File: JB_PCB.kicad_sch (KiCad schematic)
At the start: 11 parts, among them J2 Screw_Terminal_01x02, J3 Screw_Terminal_01x02, J4 Screw_Terminal_01x02, J6 Screw_Terminal_01x02

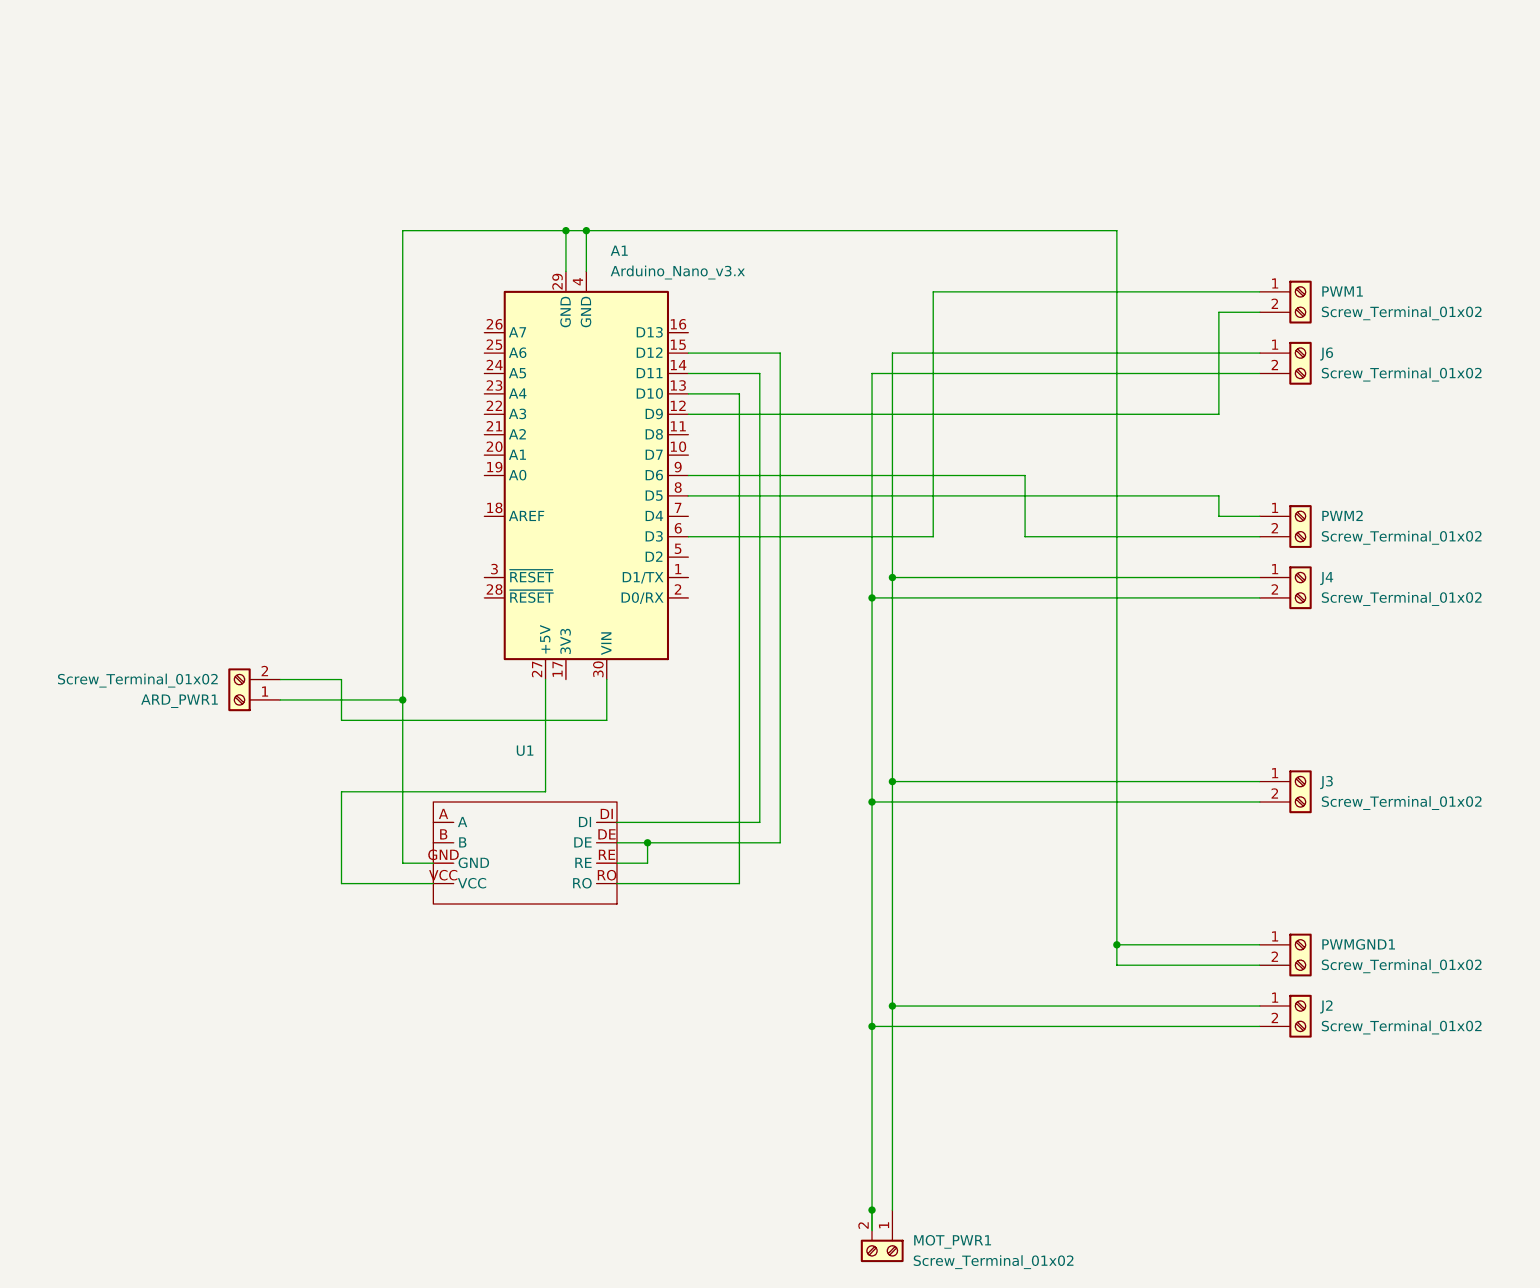
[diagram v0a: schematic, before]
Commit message: Added Servo pins
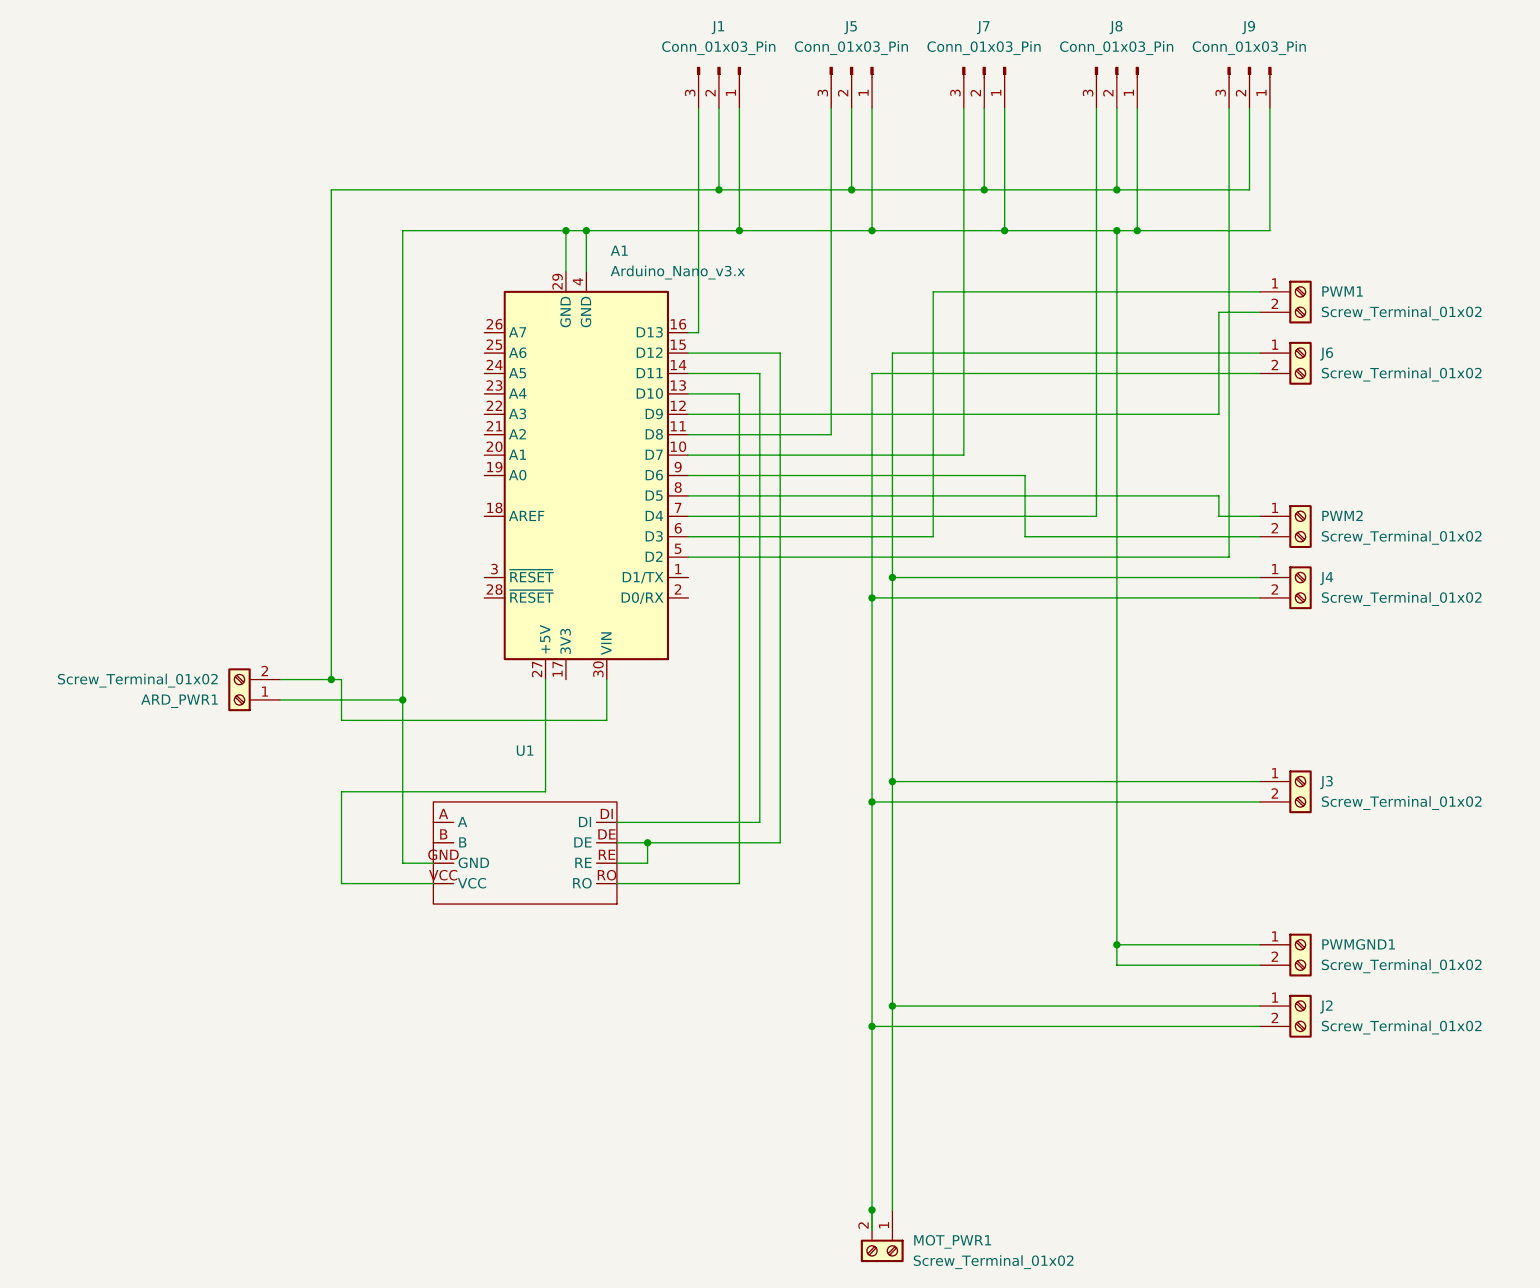
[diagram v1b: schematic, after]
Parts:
- added J1, J5, J7, J8, J9: Conn_01x03_Pin, myFootprints.pretty-master:3x1_Pin_Header, symbol Connector:Conn_01x03_Pin
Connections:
- net at A1.29 (GND), A1.4 (GND), ARD_PWR1.1 (Pin_1)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: now also J1.1 (Pin_1), J5.1 (Pin_1), J7.1 (Pin_1), J8.1 (Pin_1), J9.1 (Pin_1)
- net at A1.30 (VIN), ARD_PWR1.2 (Pin_2): now also J1.2 (Pin_2), J5.2 (Pin_2), J7.2 (Pin_2), J8.2 (Pin_2), J9.2 (Pin_2)
- net at A1.10 (D7): now also J7.3 (Pin_3)
- net at A1.11 (D8): now also J5.3 (Pin_3)
- net at A1.16 (D13): now also J1.3 (Pin_3)
- net at A1.5 (D2): now also J9.3 (Pin_3)
- net at A1.7 (D4): now also J8.3 (Pin_3)

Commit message: added pins for external PWM board
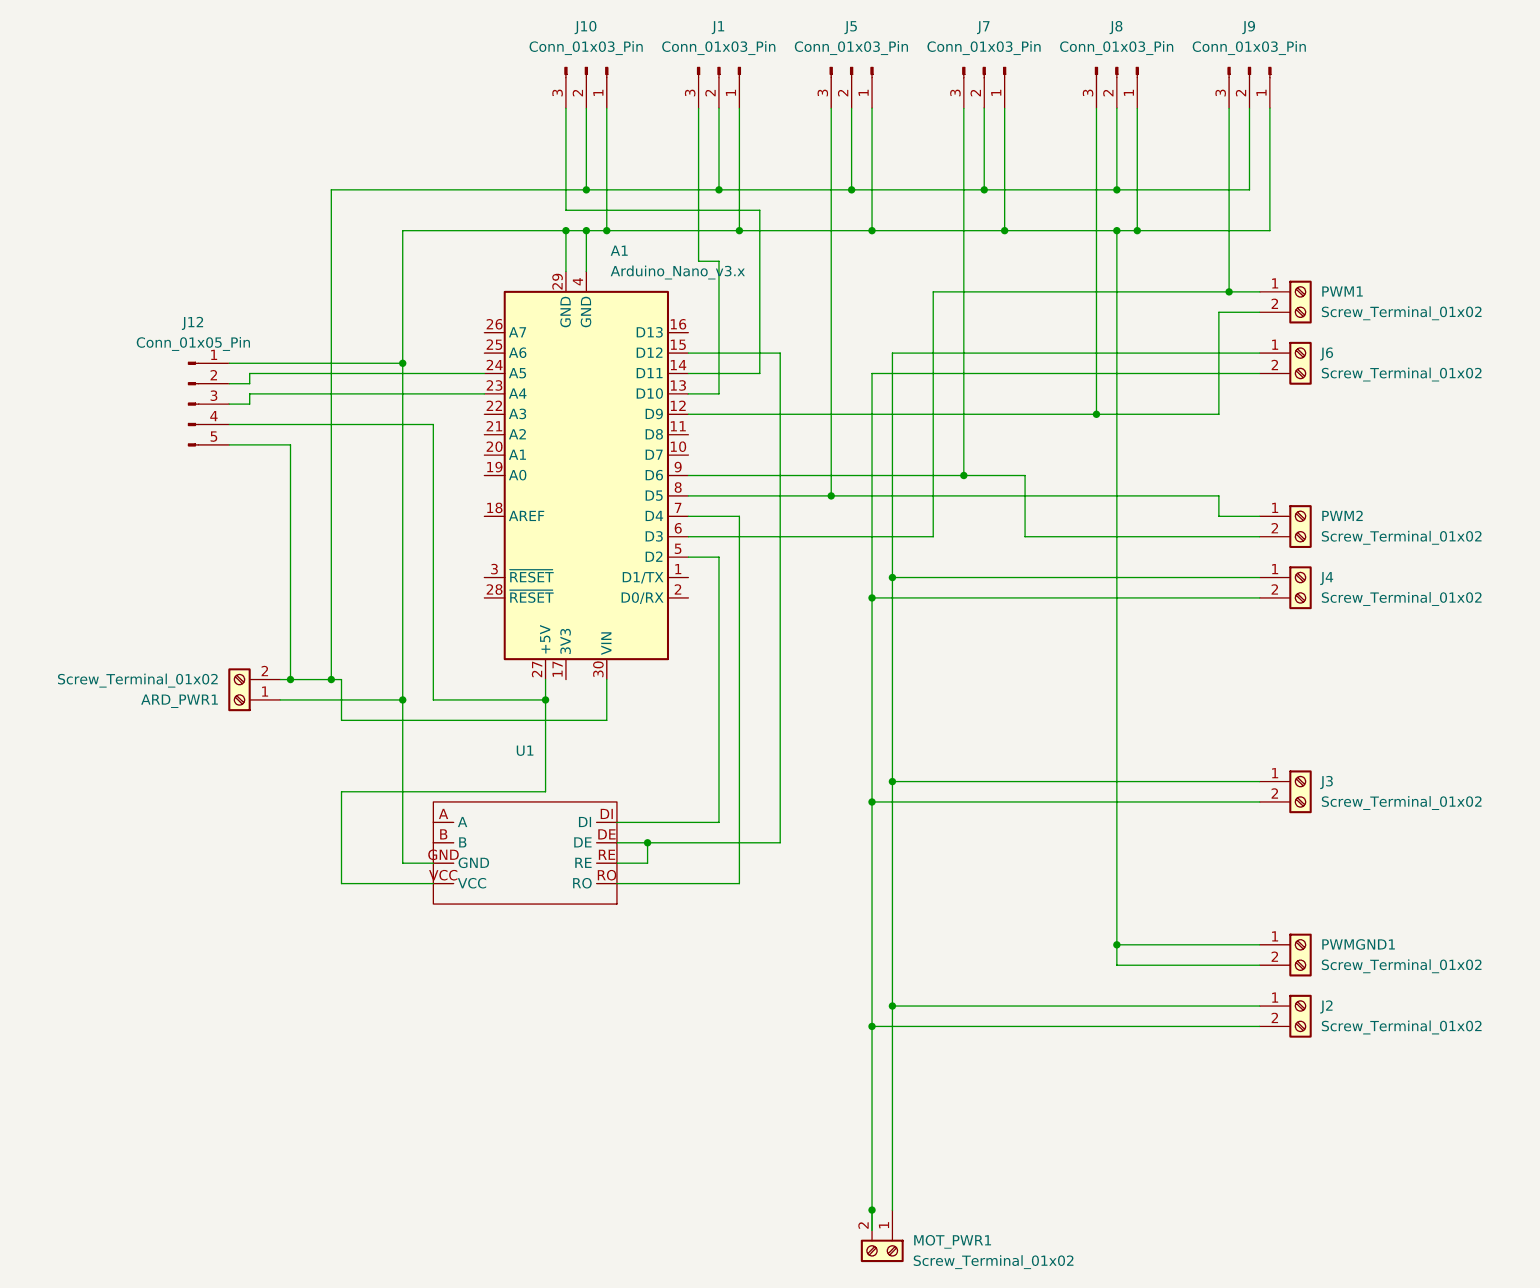
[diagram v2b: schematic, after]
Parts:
- added J10: Conn_01x03_Pin, myFootprints.pretty-master:3x1_Pin_Header, symbol Connector:Conn_01x03_Pin
- added J12: Conn_01x05_Pin, myFootprints.pretty-master:1x5conn, symbol Connector:Conn_01x05_Pin
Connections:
- net at A1.8 (D5), PWM2.1 (Pin_1): now also J5.3 (Pin_3)
- net at A1.9 (D6), PWM2.2 (Pin_2): now also J7.3 (Pin_3)
- net at A1.29 (GND), A1.4 (GND), ARD_PWR1.1 (Pin_1)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: now also J10.1 (Pin_1), J12.1 (Pin_1)
- net at A1.30 (VIN), ARD_PWR1.2 (Pin_2), J1.2 (Pin_2)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: now also J10.2 (Pin_2), J12.5 (Pin_5)
- net at A1.10 (D7): no longer J7.3 (Pin_3)
- net at J1.3 (Pin_3): now also A1.13 (D10); no longer A1.16 (D13)
- net at A1.6 (D3), PWM1.1 (Pin_1): now also J9.3 (Pin_3)
- net at A1.12 (D9), PWM1.2 (Pin_2): now also J8.3 (Pin_3)
- net at U1.DI: now also A1.5 (D2); no longer A1.14 (D11)
- net at U1.RO: now also A1.7 (D4); no longer A1.13 (D10)
- net at A1.27 (+5V), U1.VCC: now also J12.4 (Pin_4)
- net at A1.11 (D8): no longer J5.3 (Pin_3)
- net at A1.23 (A4): now also J12.3 (Pin_3)
- net at A1.24 (A5): now also J12.2 (Pin_2)
- new net: A1.14 (D11), J10.3 (Pin_3)

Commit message: changes from my laptop from last year
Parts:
- removed J1, J10, J5, J7, J8, J9: Conn_01x03_Pin, myFootprints.pretty-master:3x1_Pin_Header, symbol Connector:Conn_01x03_Pin
- removed J12: Conn_01x05_Pin, myFootprints.pretty-master:1x5conn, symbol Connector:Conn_01x05_Pin
- removed PWM1, PWM2, PWMGND1: Screw_Terminal_01x02, myFootprints.pretty-master:screw 2x2, symbol Connector:Screw_Terminal_01x02
- added J1: Conn_01x06_Pin, myFootprints.pretty-master:1x6Headers, symbol Connector:Conn_01x06_Pin
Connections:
- net at A1.29 (GND), ARD_PWR1.1 (Pin_1), U1.GND: now also J1.1 (Pin_1); no longer A1.4 (GND)
- net at A1.30 (VIN), ARD_PWR1.2 (Pin_2): now also J1.6 (Pin_6)
- net at U1.DE, U1.RE: now also A1.16 (D13); no longer A1.15 (D12)
- net at U1.DI: now also A1.15 (D12); no longer A1.5 (D2)
- net at U1.RO: now also A1.11 (D8); no longer A1.7 (D4)
- net at A1.27 (+5V), U1.VCC: now also J1.5 (Pin_5)
- net at A1.24 (A5): now also J1.3 (Pin_3)
- net at A1.23 (A4): now also J1.4 (Pin_4)
